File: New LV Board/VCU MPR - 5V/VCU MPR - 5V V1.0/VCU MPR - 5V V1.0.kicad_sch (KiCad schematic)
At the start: 6 parts, among them J1 Conn_01x12, K1 ALF1PF12, U1 LT1117-5.0

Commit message: hype esf2 and aura
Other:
- note removed: "GLV"
- note removed: "VCU GLV"
- moved on the sheet: C1, C2, F1, K1, U1

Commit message: VCU MPR 5V
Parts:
- F1: Data sheet (none) -> https://www.digikey.com/en/products/detail/littelfuse-inc/0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; Description 2 (none) -> Fuse; Fuse (none) -> Fuse
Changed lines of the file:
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@@
 		(on_board yes)
 		(dnp no)
-		(fields_autoplaced yes)
 		(property "Reference" "F1"
 			(at 154.94 90.17 0)
@@
 			)
 		)
-		(property "Description" ""
+		(property "Description" "Fuse holder"
 			(at 154.94 96.52 0)
 			(effects
@@
 				(hide yes)
 			)
+		)
+		(property "Fuse" "Fuse"
+			(at 154.94 96.52 0)
+			(effects
+				(font
+					(size 1.27 1.27)
+				)
+				(hide yes)
+			)
+		)
+		(property "Data sheet" "https://www.digikey.com/en/products/detail/littelfuse-inc/0ATO002-V/2519126"
+			(at 154.94 96.52 0)
+			(effects
+				(font
+					(size 1.27 1.27)
+				)
+				(hide yes)
+			)
+		)
+		(property "Description 2" "Fuse"
+			(at 154.94 96.52 0)
+			(effects
+				(font
+					(size 1.27 1.27)
+				)
+				(hide yes)
+			)

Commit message: Changed some labels
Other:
- note added: "VCU GLV+ 1-3"
- note removed: "VCU + 1-3"
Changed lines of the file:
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@@
 		)
 	)
-	(text "VCU + 1-3"
+	(text "VCU GLV+ 1-3"
 		(exclude_from_sim no)
 		(at 183.896 76.2 0)

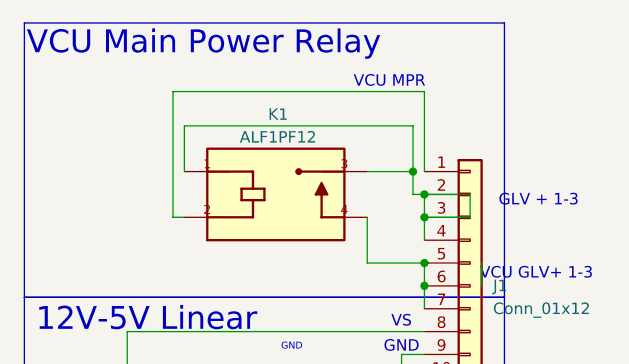
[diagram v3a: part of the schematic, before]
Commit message: fixed naming mistake.
MPR -> MPRD
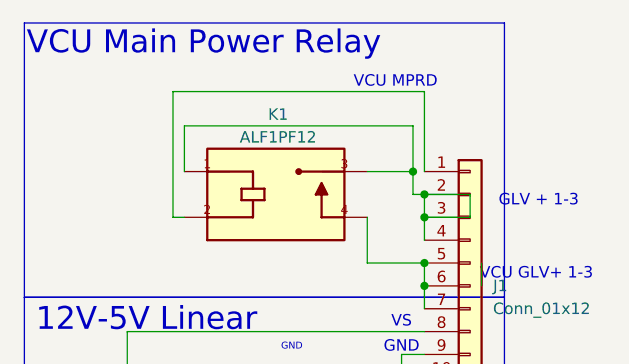
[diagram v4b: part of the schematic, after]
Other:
- note added: "VCU MPRD"
- note removed: "VCU MPR"
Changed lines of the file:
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@@
 		)
 	)
-	(text "VCU MPR\n"
+	(text "VCU MPRD\n"
 		(exclude_from_sim no)
 		(at 163.576 55.626 0)
